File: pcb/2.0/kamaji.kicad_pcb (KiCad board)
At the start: 2 copper layers, 100 x 100 mm, 84 parts, among them J1 RJ10, J2 RJ10, J3 RJ10, J4 RJ10, J5 RJ10, J6 RJ10, J7 USB_B, J8 USB_A, Q1 2N3904, Q2 IRL540N, Q3 IRL540N, SW1 SW_Push, SW2 SW_Push, SW3 SW_Push, U1 ATMEGA32U4-AU, Y1 16MHz

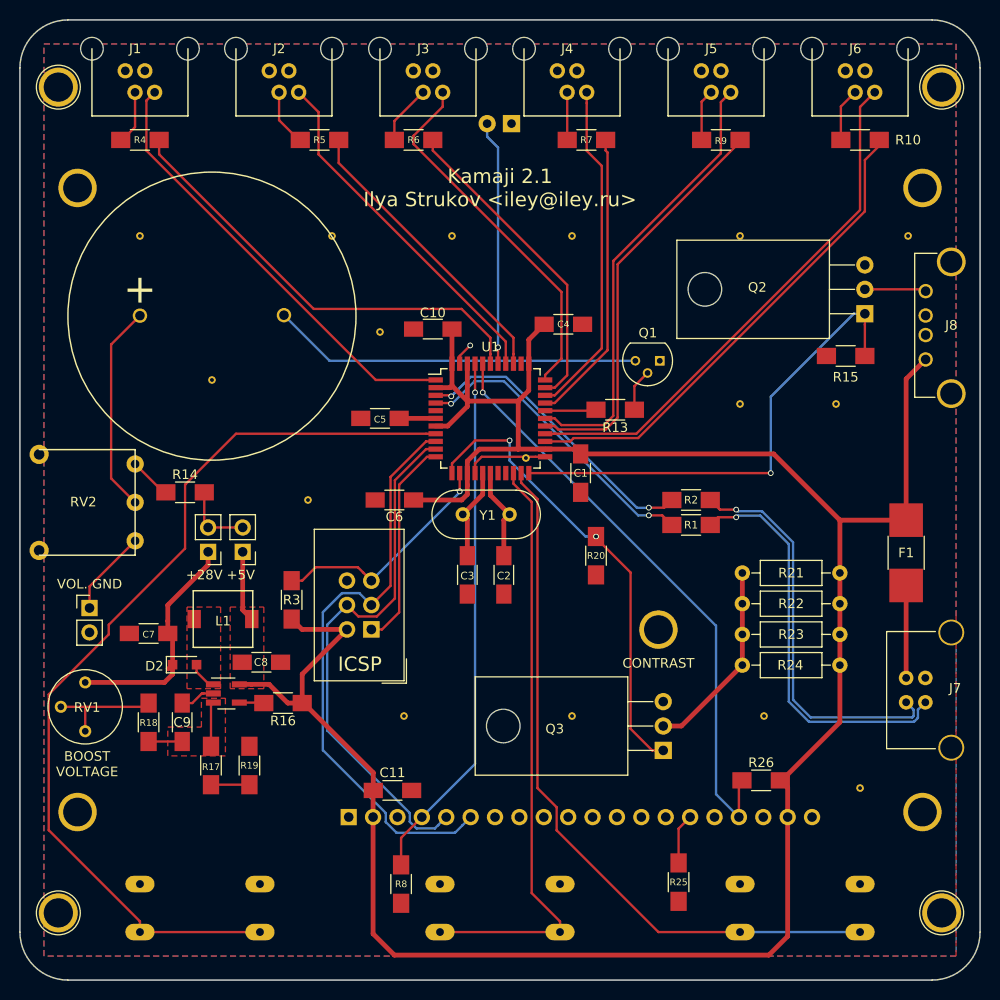
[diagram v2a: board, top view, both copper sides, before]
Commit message: move more tracks
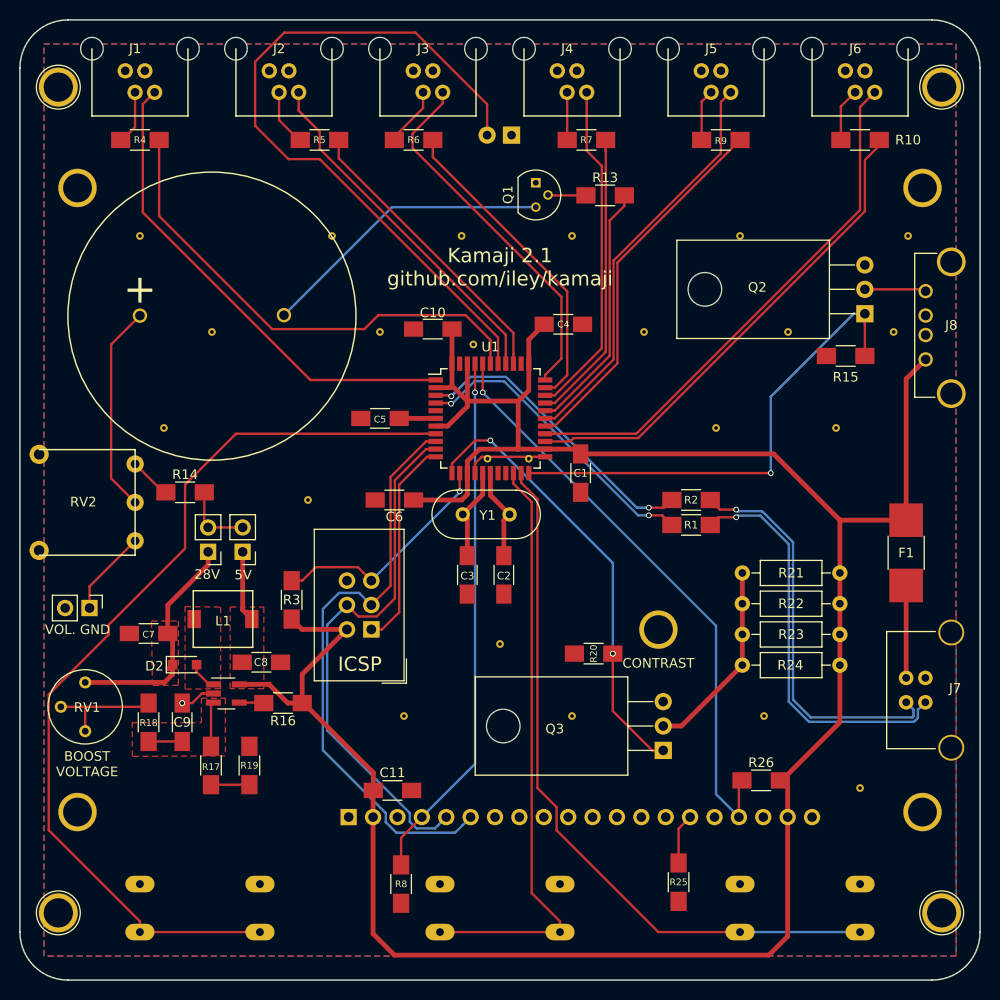
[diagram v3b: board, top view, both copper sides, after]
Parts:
- added VIA**: Via_0.8mm, kamaji:Via_0.8mm, F.Cu at (98.7, 95.7)
- added VIA**: Via_0.8mm, kamaji:Via_0.8mm, F.Cu at (65.0, 92.5)
- added VIA**: Via_0.8mm, kamaji:Via_0.8mm, F.Cu at (122.5, 92.5)
- added VIA**: Via_0.8mm, kamaji:Via_0.8mm, F.Cu at (135.0, 92.5)
- added VIA**: Via_0.8mm, kamaji:Via_0.8mm, F.Cu at (115.0, 82.5)
- added VIA**: Via_0.8mm, kamaji:Via_0.8mm, F.Cu at (100.0, 115.0)
- added VIA**: Via_0.8mm, kamaji:Via_0.8mm, F.Cu at (97.2, 83.8)
- moved Q1 22.6 mm to (103.7, 67.0), turned to 270 degrees
- moved R13 22.3 mm to (111.0, 68.3), turned to 0 degrees
- moved R20 10.2 mm to (109.8, 116.0), turned to 180 degrees
- moved VIA** 9.60 mm to (141.0, 82.5)
- moved VIA** 9.01 mm to (130.0, 82.5)
- moved VIA** 5.00 mm to (70.0, 82.5)
- moved D1 1.20 mm to (101.2, 62.0)
- moved VIA** 1.00 mm to (96.0, 72.5)
- moved VIA** 0.31 mm to (103.0, 95.7)
- turned JP1 to 270 degrees
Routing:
- net /SIGNAL_LED: track 25.5 -> 75.6 mm, vias 1 -> 0
- net /SOUND: track 5.34 -> 26.4 mm
- net Net-(LS1-Pad2): track 38.6 -> 30.9 mm
- net /PLED1: track 46.6 -> 51.4 mm
- net /PBTN1: track 46.4 -> 50.7 mm
- net /PBTN5: track 46.6 -> 42.6 mm
- net /PLED5: track 42.4 -> 39.0 mm
- net GND: track 14.6 -> 12.3 mm
- net /DUMMY_EN: track 48.2 -> 46.4 mm
- added copper zone on F.Cu, net /Boost Converter/BOOST_VOUT
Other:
- board text added: "28V"
- board text added: "5V"
- board text added: "Kamaji 2.1 github.com/iley/kamaji"
- board text removed: "+28V"
- board text removed: "+5V"
- board text removed: "Kamaji 2.1 Ilya Strukov <iley@iley.ru>"

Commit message: add a missing resistor
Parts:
- added R11: 220R, Resistors_SMD:R_1206_HandSoldering, F.Cu at (72.8, 62.5)
- R17: value 31K3 -> 13K3
- R19: value 0 -> 680R
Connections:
- D1 pad 2: /SIGNAL_LED -> Net-(D1-Pad2)
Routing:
- net Net-(D1-Pad2): track 0.00 -> 41.8 mm
- net /SIGNAL_LED: track 75.6 -> 35.8 mm
- net /PLED1: track 51.4 -> 45.4 mm
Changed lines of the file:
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@@
 (kicad_pcb (version 4) (host pcbnew 4.0.7)
   (general
-    (links 186)
-    (no_connects 1)
+    (links 187)
+    (no_connects 3)
     (area 49.924999 49.924999 150.075001 150.075001)
     (thickness 1.6)
@@
     (tracks 370)
     (zones 0)
-    (modules 91)
-    (nets 57)
+    (modules 92)
+    (nets 58)
   )
   (page A4)
@@
   (net 55 "Net-(JP1-Pad1)")
   (net 56 /DUMMY-)
+  (net 57 "Net-(D1-Pad2)")
   (net_class Default "This is the default net class."
     (clearance 0.1524)
@@
     (add_net "Net-(C3-Pad1)")
     (add_net "Net-(C5-Pad1)")
+    (add_net "Net-(D1-Pad2)")
     (add_net "Net-(DS1-Pad15)")
     (add_net "Net-(J1-Pad2)")
@@
       (effects (font (size 0.7 0.7) (thickness 0.15)))
     )
-    (fp_text value 31K3 (at 0 1.9 90) (layer F.Fab)
+    (fp_text value 13K3 (at 0 1.9 90) (layer F.Fab)
       (effects (font (size 1 1) (thickness 0.15)))
     )
@@
       (effects (font (size 0.7 0.7) (thickness 0.15)))
     )
-    (fp_text value 0 (at 0 1.9 90) (layer F.Fab)
+    (fp_text value 680R (at 0 1.9 90) (layer F.Fab)
       (effects (font (size 1 1) (thickness 0.15)))
     )
@@
       (net 49 GND))
     (pad 2 thru_hole circle (at 2.54 0 180) (size 1.8 1.8) (drill 0.9) (layers *.Cu *.Mask)
-      (net 54 /SIGNAL_LED))
+      (net 57 "Net-(D1-Pad2)"))
     (model ${KISYS3DMOD}/LEDs.3dshapes/LED_D5.0mm.wrl
       (at (xyz 0 0 0))
@@
     (pad "" np_thru_hole circle (at 0 0) (size 4.064 4.064) (drill 3.048) (layers *.Cu *.Mask))
   )
+  (module Resistors_SMD:R_1206_HandSoldering (layer F.Cu)
+    (at 72.85 62.45)
+    (descr "Resistor SMD 1206, hand soldering")
+    (tags "resistor 1206")
+    (attr smd)
+    (fp_text reference R11 (at 0 -1.85) (layer F.SilkS)
+      (effects (font (size 1 1) (thickness 0.15)))
+    )
+    (fp_text value 220R (at 0 1.9) (layer F.Fab)
+      (effects (font (size 1 1) (thickness 0.15)))
+    )
+    (fp_text user %R (at 0 0) (layer F.Fab)
+      (effects (font (size 0.7 0.7) (thickness 0.105)))
+    )
+    (fp_line (start -1.6 0.8) (end -1.6 -0.8) (layer F.Fab) (width 0.1))
+    (fp_line (start 1.6 0.8) (end -1.6 0.8) (layer F.Fab) (width 0.1))
+    (fp_line (start 1.6 -0.8) (end 1.6 0.8) (layer F.Fab) (width 0.1))
+    (fp_line (start -1.6 -0.8) (end 1.6 -0.8) (layer F.Fab) (width 0.1))
+    (fp_line (start 1 1.07) (end -1 1.07) (layer F.SilkS) (width 0.12))
+    (fp_line (start -1 -1.07) (end 1 -1.07) (layer F.SilkS) (width 0.12))
+    (fp_line (start -3.25 -1.11) (end 3.25 -1.11) (layer F.CrtYd) (width 0.05))
+    (fp_line (start -3.25 -1.11) (end -3.25 1.1) (layer F.CrtYd) (width 0.05))
+    (fp_line (start 3.25 1.1) (end 3.25 -1.11) (layer F.CrtYd) (width 0.05))
+    (fp_line (start 3.25 1.1) (end -3.25 1.1) (layer F.CrtYd) (width 0.05))
+    (pad 1 smd rect (at -2 0) (size 2 1.7) (layers F.Cu F.Paste F.Mask)
+      (net 57 "Net-(D1-Pad2)"))
+    (pad 2 smd rect (at 2 0) (size 2 1.7) (layers F.Cu F.Paste F.Mask)
+      (net 54 /SIGNAL_LED))
+    (model ${KISYS3DMOD}/Resistors_SMD.3dshapes/R_1206.wrl
+      (at (xyz 0 0 0))
+      (scale (xyz 1 1 1))
+      (rotate (xyz 0 0 0))
+    )
+  )
   (gr_text CONTRAST (at 116.5 117) (layer F.SilkS)
     (effects (font (size 1 1) (thickness 0.2)))
@@
   (segment (start 76.99 60.44) (end 79.05 62.5) (width 0.25) (layer F.Cu) (net 15))
   (segment (start 79.05 62.5) (end 79.2 62.5) (width 0.25) (layer F.Cu) (net 15))
-  (segment (start 79.03 57.53) (end 79.03 59.455) (width 0.25) (layer F.Cu) (net 16))
-  (segment (start 79.03 59.455) (end 81.225 61.65) (width 0.25) (layer F.Cu) (net 16))
-  (segment (start 81.225 61.65) (end 81.225 63.425) (width 0.25) (layer F.Cu) (net 16))
-  (segment (start 81.225 63.425) (end 100.6 82.8) (width 0.25) (layer F.Cu) (net 16))
+  (segment (start 79.03 57.53) (end 81.225 59.725) (width 0.25) (layer F.Cu) (net 16))
+  (segment (start 81.225 59.725) (end 81.225 64.375) (width 0.25) (layer F.Cu) (net 16))
+  (segment (start 81.225 64.375) (end 100.6 83.75) (width 0.25) (layer F.Cu) (net 16))
+  (segment (start 100.6 83.75) (end 100.6 84.8) (width 0.25) (layer F.Cu) (net 16))
   (segment (start 100.6 84.8) (end 100.6 85.8) (width 0.25) (layer F.Cu) (net 16))
-  (segment (start 100.6 82.8) (end 100.6 84.8) (width 0.25) (layer F.Cu) (net 16))
   (segment (start 89 62.5) (end 89 62.175) (width 0.25) (layer F.Cu) (net 17))
   (segment (start 91.99 59.185) (end 91.99 57.54) (width 0.25) (layer F.Cu) (net 17))
@@
   (segment (start 111.75 121.98) (end 111.75 117.1) (width 0.25) (layer F.Cu) (net 33))
   (segment (start 111.75 117.1) (end 111.75 116) (width 0.25) (layer F.Cu) (net 33))
-  (segment (start 64.5 62.5) (end 64.5 70.425) (width 0.25) (layer F.Cu) (net 34))
-  (segment (start 64.5 70.425) (end 76.275 82.2) (width 0.25) (layer F.Cu) (net 34))
-  (segment (start 76.275 82.2) (end 85.875 82.2) (width 0.25) (layer F.Cu) (net 34))
-  (segment (start 85.875 82.2) (end 87.325 80.75) (width 0.25) (layer F.Cu) (net 34))
-  (segment (start 87.325 80.75) (end 96.425 80.75) (width 0.25) (layer F.Cu) (net 34))
-  (segment (start 96.425 80.75) (end 99 83.325) (width 0.25) (layer F.Cu) (net 34))
-  (segment (start 99 83.325) (end 99 85.8) (width 0.25) (layer F.Cu) (net 34))
-  (segment (start 83.2 62.5) (end 83.2 64.4) (width 0.25) (layer F.Cu) (net 35))
-  (segment (start 83.2 64.4) (end 101.4 82.6) (width 0.25) (layer F.Cu) (net 35))
-  (segment (start 101.4 82.6) (end 101.4 84.8) (width 0.25) (layer F.Cu) (net 35))
+  (segment (start 99 84.8) (end 99 85.8) (width 0.25) (layer F.Cu) (net 34))
+  (segment (start 84 80.75) (end 96.030906 80.75) (width 0.25) (layer F.Cu) (net 34))
+  (segment (start 65.75 62.5) (end 84 80.75) (width 0.25) (layer F.Cu) (net 34))
+  (segment (start 64.5 62.5) (end 65.75 62.5) (width 0.25) (layer F.Cu) (net 34))
+  (segment (start 99 83.719094) (end 99 84.8) (width 0.25) (layer F.Cu) (net 34))
+  (segment (start 96.030906 80.75) (end 99 83.719094) (width 0.25) (layer F.Cu) (net 34))
+  (segment (start 83.2 62.5) (end 83.2 65.65) (width 0.25) (layer F.Cu) (net 35))
+  (segment (start 83.2 65.65) (end 101.4 83.85) (width 0.25) (layer F.Cu) (net 35))
+  (segment (start 101.4 83.85) (end 101.4 84.8) (width 0.25) (layer F.Cu) (net 35))
   (segment (start 101.4 84.8) (end 101.4 85.8) (width 0.25) (layer F.Cu) (net 35))
   (segment (start 93 62.5) (end 93 64.275) (width 0.25) (layer F.Cu) (net 36))
@@
   (segment (start 144.3 121.07) (end 143.524999 121.845001) (width 0.25) (layer B.Cu) (net 53))
   (segment (start 143.524999 121.845001) (end 143.524999 122.693199) (width 0.25) (layer B.Cu) (net 53))
-  (segment (start 98.66 59.527208) (end 98.66 62) (width 0.25) (layer F.Cu) (net 54))
-  (segment (start 99.8 85.8) (end 99.8 83.075) (width 0.25) (layer F.Cu) (net 54))
-  (segment (start 99.8 83.075) (end 81.225 64.5) (width 0.25) (layer F.Cu) (net 54))
-  (segment (start 77.525 51.325) (end 91.2 51.325) (width 0.25) (layer F.Cu) (net 54))
-  (segment (start 81.225 64.5) (end 77.975 64.5) (width 0.25) (layer F.Cu) (net 54))
-  (segment (start 77.975 64.5) (end 74.5 61.025) (width 0.25) (layer F.Cu) (net 54))
-  (segment (start 74.5 61.025) (end 74.5 54.35) (width 0.25) (layer F.Cu) (net 54))
-  (segment (start 74.5 54.35) (end 77.525 51.325) (width 0.25) (layer F.Cu) (net 54))
-  (segment (start 91.2 51.325) (end 98.66 58.785) (width 0.25) (layer F.Cu) (net 54))
-  (segment (start 98.66 58.785) (end 98.66 59.527208) (width 0.25) (layer F.Cu) (net 54))
+  (segment (start 99.8 85.8) (end 99.8 83.75) (width 0.25) (layer F.Cu) (net 54))
+  (segment (start 80.6 64.55) (end 78.2 64.55) (width 0.25) (layer F.Cu) (net 54))
+  (segment (start 99.8 83.75) (end 80.6 64.55) (width 0.25) (layer F.Cu) (net 54))
+  (segment (start 78.2 64.55) (end 76.1 62.45) (width 0.25) (layer F.Cu) (net 54))
+  (segment (start 76.1 62.45) (end 74.85 62.45) (width 0.25) (layer F.Cu) (net 54))
   (segment (start 62 104.25) (end 57.25 109) (width 0.25) (layer F.Cu) (net 55))
   (segment (start 57.25 109) (end 57.25 111.25) (width 0.25) (layer F.Cu) (net 55))
@@
   (segment (start 117 123.54) (end 118.9 123.54) (width 0.5) (layer F.Cu) (net 56))
   (segment (start 118.9 123.54) (end 125.24 117.2) (width 0.5) (layer F.Cu) (net 56))
+  (segment (start 70.85 62.45) (end 70.85 57.8) (width 0.25) (layer F.Cu) (net 57))
+  (segment (start 70.85 57.8) (end 77.35 51.3) (width 0.25) (layer F.Cu) (net 57))
+  (segment (start 77.35 51.3) (end 91.45 51.3) (width 0.25) (layer F.Cu) (net 57))
+  (segment (start 98.66 60.727208) (end 98.66 62) (width 0.25) (layer F.Cu) (net 57))
+  (segment (start 91.45 51.3) (end 98.66 58.51) (width 0.25) (layer F.Cu) (net 57))
+  (segment (start 98.66 58.51) (end 98.66 60.727208) (width 0.25) (layer F.Cu) (net 57))
+  (segment (start 79.8 70.25) (end 79.65 70.25) (width 0.25) (layer F.Cu) (net 57))
   (zone (net 49) (net_name GND) (layer B.Cu) (hatch edge 0.508)
     (connect_pads (clearance 0.3))

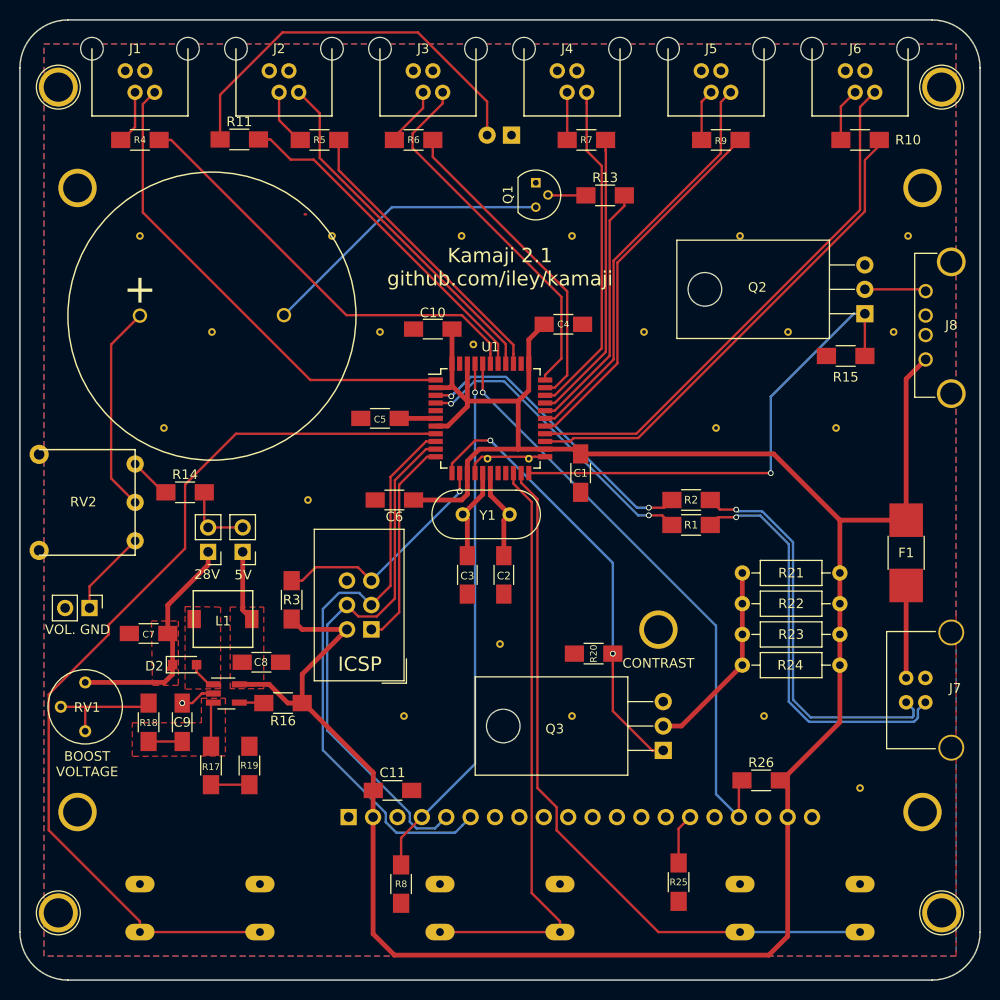
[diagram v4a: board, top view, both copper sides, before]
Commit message: fix track clearance
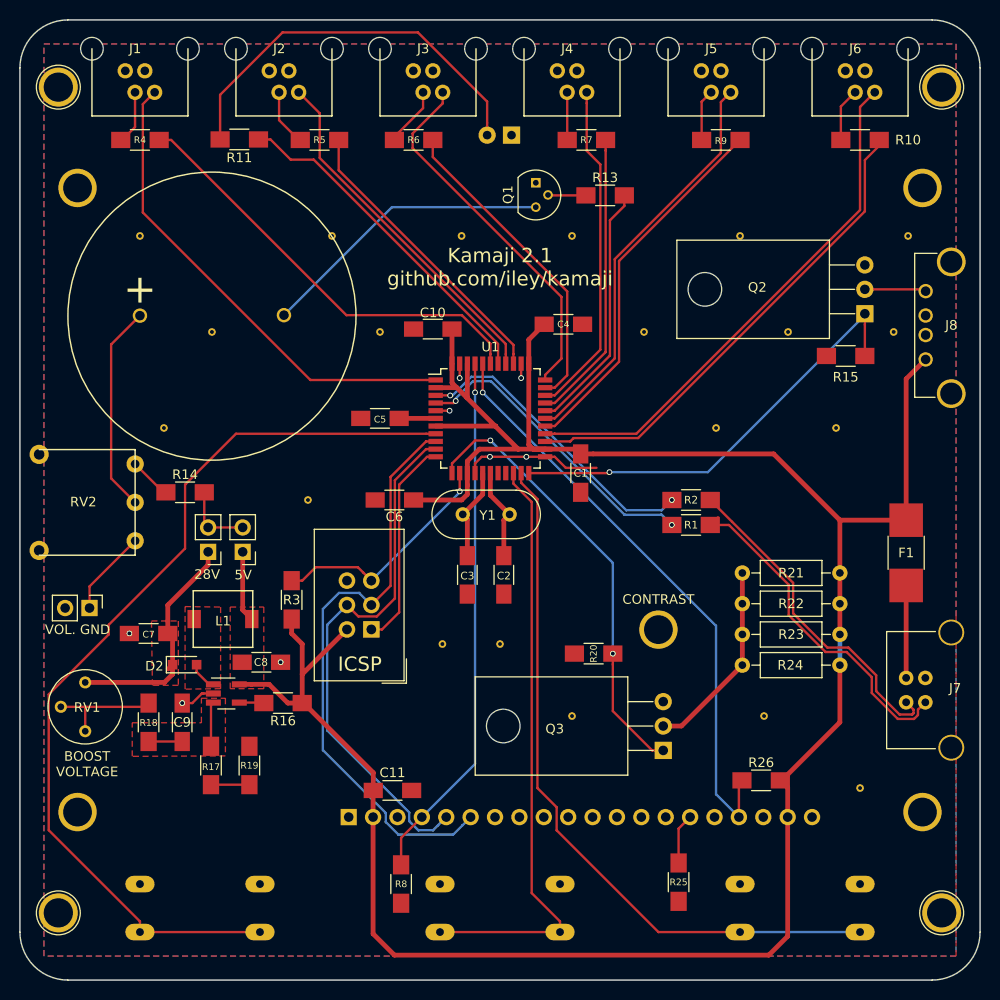
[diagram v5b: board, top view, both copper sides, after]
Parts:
- removed the VIA** at (98.7, 95.7)
- removed the VIA** at (97.2, 83.8)
- removed the VIA** at (103.0, 95.7)
- moved VIA** 8.50 mm to (94.0, 115.0)
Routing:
- net GND: track 12.3 -> 22.5 mm, vias 1 -> 8
- net /USBBD-: track 42.0 -> 34.8 mm, vias 1 -> 0
- net /USBBD+: track 42.6 -> 35.8 mm, vias 1 -> 0
- net /LAMP: track 50.9 -> 46.4 mm
- net VCC: track 263.1 -> 267.6 mm
- net /USB_D-: track 31.5 -> 32.7 mm
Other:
- net class Default: clearance 0.1524 -> 0.2
- rule trace_clearance: 0.1524 -> 0.2

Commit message: a few minor PCB changes
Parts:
- removed the VIA** at (65.0, 92.5)
- removed the VIA** at (87.5, 82.5)
- ICSP1: footprint Connectors_IDC:IDC-Header_2x03_Pitch2.54mm_Straight -> kamaji:ATmega_ISP_6pin
- moved VIA** 3.84 mm to (72.4, 85.5)
- moved C5 3.83 mm to (90.7, 89.4), turned to 90 degrees
- moved C6 2.84 mm to (91.2, 101.8), turned to 270 degrees
- moved ICSP1 2.84 mm to (85.3, 110.9), turned to 90 degrees
- moved C4 1.40 mm to (106.7, 83.1)
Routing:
- net GND: track 22.5 -> 34.2 mm, vias 8 -> 12
- net /MOSI: track 55.9 -> 61.8 mm
- net /SCK: track 61.7 -> 66.3 mm
- net VCC: track 267.6 -> 265.3 mm
- net /PBTN1: track 50.7 -> 52.4 mm
- net Net-(C5-Pad1): track 3.80 -> 2.64 mm
- net /RST: track 24.5 -> 25.1 mm
- net /SIGNAL_LED: track 35.8 -> 36.5 mm
- net /PLED1: track 45.4 -> 46.0 mm
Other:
- board text added: "ISP"
- board text removed: "ICSP"
